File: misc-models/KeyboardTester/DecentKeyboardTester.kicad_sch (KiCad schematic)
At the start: 53 parts, among them J1 Conn_01x24, J10 Conn_01x03, J11 Conn_2Rows-15Pins, J2 Conn_01x18, J3 Conn_01x22, J4 Conn_01x15, J5 SM03B-SRSS-TB, J6 USB_B_Micro, J7 Barrel_Jack, J8 Conn_01x04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

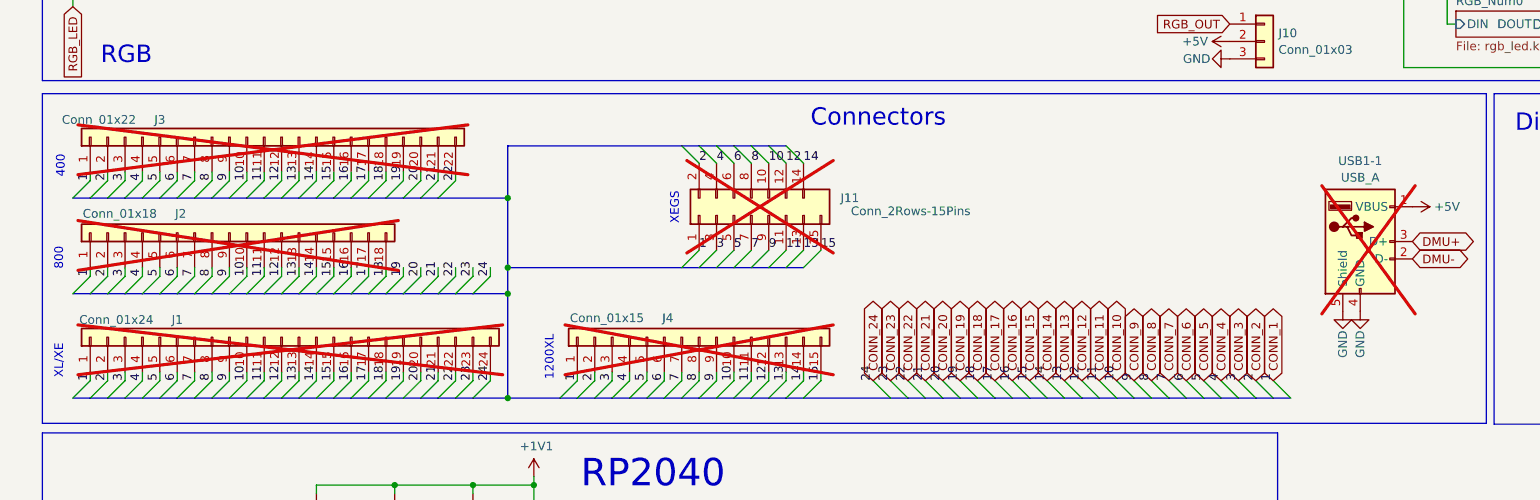
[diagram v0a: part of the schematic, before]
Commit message: Atari 800 keyboard support in the tester
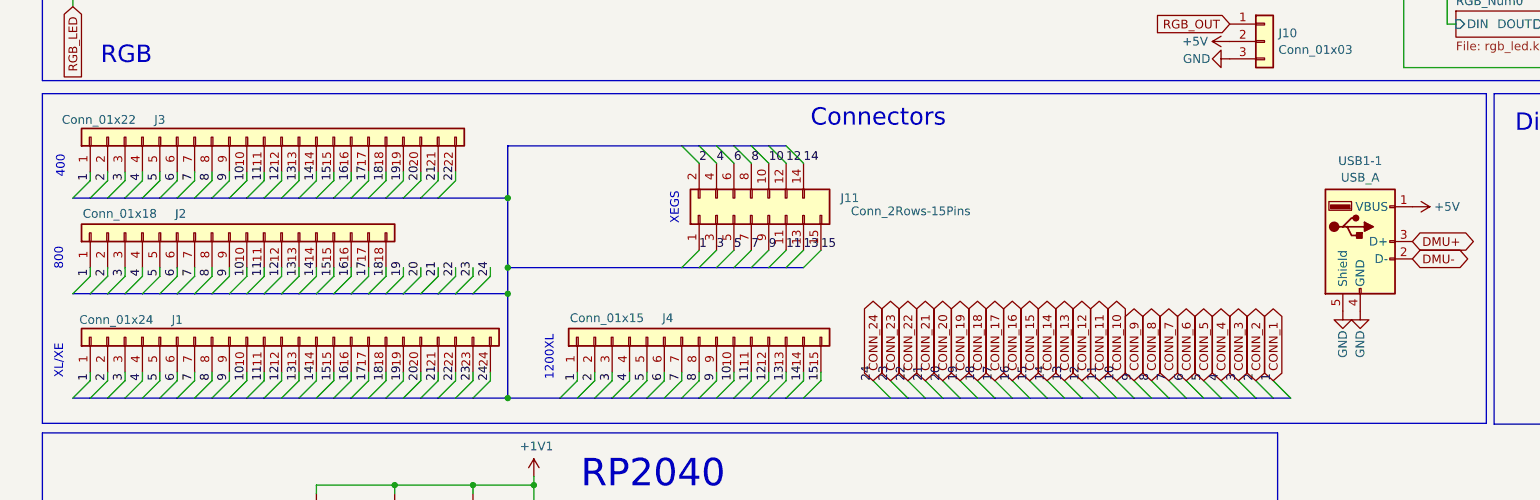
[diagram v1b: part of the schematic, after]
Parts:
- J1, J11, J2, J3, J4, USB1-1: now fitted
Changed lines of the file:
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@@
 		(in_bom yes)
 		(on_board yes)
-		(dnp yes)
+		(dnp no)
 		(property "Reference" "J1"
 			(at 33.02 168.91 90)
@@
 		(in_bom yes)
 		(on_board yes)
-		(dnp yes)
+		(dnp no)
 		(property "Reference" "J4"
 			(at 104.648 168.656 90)
@@
 		(in_bom yes)
 		(on_board yes)
-		(dnp yes)
+		(dnp no)
 		(property "Reference" "J2"
 			(at 33.528 153.416 90)
@@
 		(in_bom yes)
 		(on_board yes)
-		(dnp yes)
+		(dnp no)
 		(property "Reference" "J3"
 			(at 30.48 139.7 90)
@@
 		(in_bom yes)
 		(on_board yes)
-		(dnp yes)
+		(dnp no)
 		(property "Reference" "J11"
 			(at 132.588 151.13 90)
@@
 		(in_bom yes)
 		(on_board yes)
-		(dnp yes)
+		(dnp no)
 		(fields_autoplaced yes)
 		(property "Reference" "USB1-1"
